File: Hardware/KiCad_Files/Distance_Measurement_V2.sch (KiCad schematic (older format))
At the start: 8 parts, among them J1 Conn_01x04_Female, J2 Screw_Terminal_01x02, Q1 2N5109, U1 WeMos_D1_mini

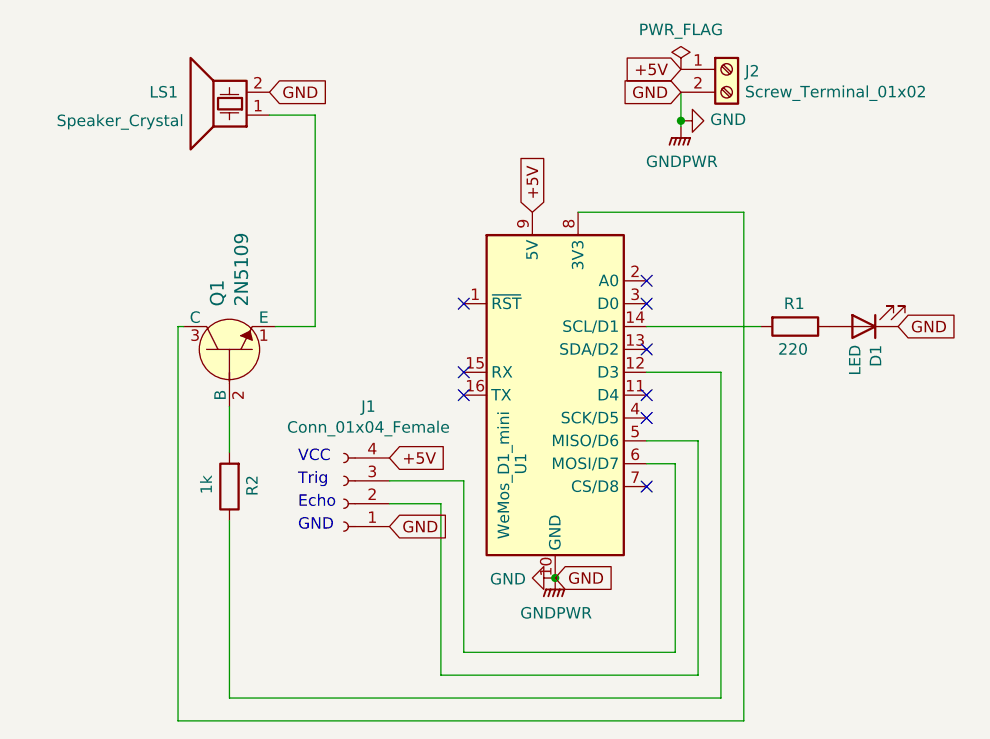
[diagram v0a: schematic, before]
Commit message: added Version 2
including a battery holder for 18650
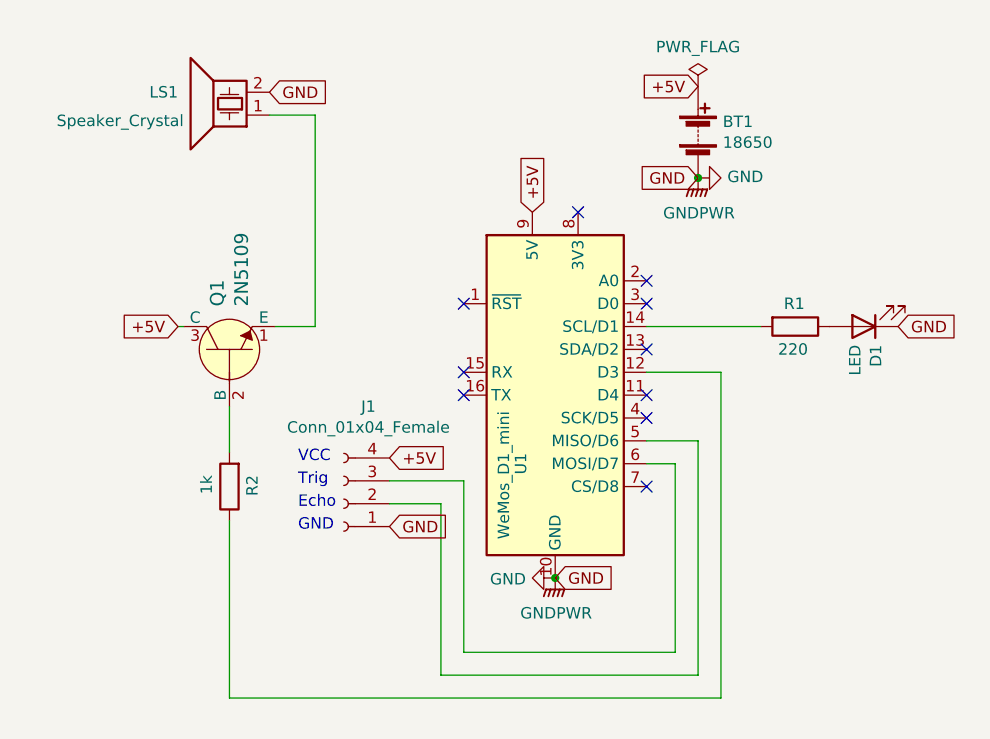
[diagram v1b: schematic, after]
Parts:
- removed J2: Screw_Terminal_01x02, TerminalBlock_Phoenix:TerminalBlock_Phoenix_MPT-0,5-2-2.54_1x02_P2.54mm_Horizontal, symbol Connector:Screw_Terminal_01x02
- added BT1: 18650, Battery:BatteryHolder_MPD_BH-18650-PC2, symbol Device:Battery
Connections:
- net +5V: now also Q1.3 (C), BT1.1 (+)
- net GND: now also BT1.2 (-)
- net at U1.8 (3V3): no longer Q1.3 (C)
- no-connect marks 9 -> 10
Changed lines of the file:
@@
 Sheet 1 1
 Title "WemosD1 mini Distance Measurement"
-Date "2021-11-11"
-Rev "Rev. 02"
+Date "2021-11-27"
+Rev "Version 2 Rev. 01"
 Comp "Emilia & Papa"
 Comment1 ""
@@
 	-1   0    0    1
 $EndComp
-$Comp
-L Connector:Screw_Terminal_01x02 J2
-U 1 1 616C480C
-P 6500 1975
-F 0 "J2" H 6580 1967 50  0000 L CNN
-F 1 "Screw_Terminal_01x02" H 6580 1876 50  0000 L CNN
-F 2 "TerminalBlock_Phoenix:TerminalBlock_Phoenix_MPT-0,5-2-2.54_1x02_P2.54mm_Horizontal" H 6500 1975 50  0001 C CNN
-F 3 "~" H 6500 1975 50  0001 C CNN
-	1    6500 1975
-	1    0    0    -1
-$EndComp
-Text GLabel 6300 1975 0    50   Input ~ 0
-+5V
-Text GLabel 6300 2075 0    50   Input ~ 0
-GND
+Text GLabel 6375 2050 0    50   Input ~ 0
++5V
 $Comp
 L power:PWR_FLAG #FLG01
 U 1 1 616CBB59
-P 6300 1975
-F 0 "#FLG01" H 6300 2050 50  0001 C CNN
-F 1 "PWR_FLAG" H 6300 2148 50  0000 C CNN
-F 2 "" H 6300 1975 50  0001 C CNN
-F 3 "~" H 6300 1975 50  0001 C CNN
-	1    6300 1975
+P 6375 2050
+F 0 "#FLG01" H 6375 2125 50  0001 C CNN
+F 1 "PWR_FLAG" H 6375 2223 50  0000 C CNN
+F 2 "" H 6375 2050 50  0001 C CNN
+F 3 "~" H 6375 2050 50  0001 C CNN
+	1    6375 2050
 	1    0    0    -1
 $EndComp
@@
 NoConn ~ 6150 3400
 NoConn ~ 6150 3500
-Text GLabel 5750 4200 2    50   Input ~ 0
-GND
 Text Notes 4625 3700 0    50   ~ 0
 VCC
@@
 Text GLabel 5025 3975 2    50   Input ~ 0
 GND
-Wire Wire Line
-	6375 3600 6375 4625
 Wire Wire Line
 	6375 4625 5250 4625
@@
 Wire Wire Line
 	4325 4725 6475 4725
-$Comp
-L power:GNDPWR #PWR0101
-U 1 1 616FD5B6
-P 6300 2225
-F 0 "#PWR0101" H 6300 2025 50  0001 C CNN
-F 1 "GNDPWR" H 6304 2071 50  0000 C CNN
-F 2 "" H 6300 2175 50  0001 C CNN
-F 3 "" H 6300 2175 50  0001 C CNN
-	1    6300 2225
-	1    0    0    -1
-$EndComp
-Wire Wire Line
-	6300 2225 6300 2200
-$Comp
-L power:GND #PWR0102
-U 1 1 616FF170
-P 6300 2200
-F 0 "#PWR0102" H 6300 1950 50  0001 C CNN
-F 1 "GND" V 6305 2072 50  0000 R CNN
-F 2 "" H 6300 2200 50  0001 C CNN
-F 3 "" H 6300 2200 50  0001 C CNN
-	1    6300 2200
-	0    -1   -1   0
-$EndComp
-Connection ~ 6300 2200
-Wire Wire Line
-	6300 2200 6300 2075
-$Comp
-L power:GND #PWR0103
-U 1 1 616FFAE5
-P 5750 4200
-F 0 "#PWR0103" H 5750 3950 50  0001 C CNN
-F 1 "GND" V 5755 4072 50  0000 R CNN
-F 2 "" H 5750 4200 50  0001 C CNN
-F 3 "" H 5750 4200 50  0001 C CNN
-	1    5750 4200
-	0    1    1    0
-$EndComp
-$Comp
-L power:GNDPWR #PWR0104
-U 1 1 617003F6
-P 5750 4200
-F 0 "#PWR0104" H 5750 4000 50  0001 C CNN
-F 1 "GNDPWR" H 5754 4046 50  0000 C CNN
-F 2 "" H 5750 4150 50  0001 C CNN
-F 3 "" H 5750 4150 50  0001 C CNN
-	1    5750 4200
-	1    0    0    -1
-$EndComp
-Connection ~ 5750 4200
 Text GLabel 7250 3100 2    50   Input ~ 0
 GND
-Wire Wire Line
-	5850 2600 6575 2600
-Wire Wire Line
-	6575 2600 6575 4825
-Wire Wire Line
-	6575 4825 4100 4825
-Wire Wire Line
-	4100 4825 4100 3100
 Wire Wire Line
 	4500 2175 4700 2175
@@
 Wire Wire Line
 	6650 3100 6150 3100
+Text GLabel 4100 3100 0    50   Input ~ 0
++5V
+NoConn ~ 5850 2600
+$Comp
+L Device:Battery BT1
+U 1 1 61A1E8BC
+P 6375 2250
+F 0 "BT1" H 6483 2296 50  0000 L CNN
+F 1 "18650" H 6483 2205 50  0000 L CNN
+F 2 "Battery:BatteryHolder_MPD_BH-18650-PC2" H 6483 2159 50  0001 L CNN
+F 3 "~" V 6375 2310 50  0001 C CNN
+	1    6375 2250
+	1    0    0    -1
+$EndComp
+Wire Wire Line
+	6375 3600 6375 4625
+$Comp
+L power:GND #PWR0102
+U 1 1 616FF170
+P 6375 2450
+F 0 "#PWR0102" H 6375 2200 50  0001 C CNN
+F 1 "GND" V 6380 2322 50  0000 R CNN
+F 2 "" H 6375 2450 50  0001 C CNN
+F 3 "" H 6375 2450 50  0001 C CNN
+	1    6375 2450
+	0    -1   -1   0
+$EndComp
+$Comp
+L power:GND #PWR0103
+U 1 1 616FFAE5
+P 5750 4200
+F 0 "#PWR0103" H 5750 3950 50  0001 C CNN
+F 1 "GND" V 5755 4072 50  0000 R CNN
+F 2 "" H 5750 4200 50  0001 C CNN
+F 3 "" H 5750 4200 50  0001 C CNN
+	1    5750 4200
+	0    1    1    0
+$EndComp
+Text GLabel 5750 4200 2    50   Input ~ 0
+GND
+Connection ~ 5750 4200
+$Comp
+L power:GNDPWR #PWR0104
+U 1 1 617003F6
+P 5750 4200
+F 0 "#PWR0104" H 5750 4000 50  0001 C CNN
+F 1 "GNDPWR" H 5754 4046 50  0000 C CNN
+F 2 "" H 5750 4150 50  0001 C CNN
+F 3 "" H 5750 4150 50  0001 C CNN
+	1    5750 4200
+	1    0    0    -1
+$EndComp
+Connection ~ 6375 2450
+$Comp
+L power:GNDPWR #PWR0101
+U 1 1 616FD5B6
+P 6375 2450
+F 0 "#PWR0101" H 6375 2250 50  0001 C CNN
+F 1 "GNDPWR" H 6379 2296 50  0000 C CNN
+F 2 "" H 6375 2400 50  0001 C CNN
+F 3 "" H 6375 2400 50  0001 C CNN
+	1    6375 2450
+	1    0    0    -1
+$EndComp
+Text GLabel 6375 2450 0    50   Input ~ 0
+GND
 $EndSCHEMATC
